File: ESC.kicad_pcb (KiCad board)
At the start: 2 copper layers, 44.5 x 36 mm, 68 parts, among them U1 DRV8300DRGER, U10 AP7381-33SA-7, U8 STM32G071GBU3TR, U9 UA78L10ACPK

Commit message: Fixed pin names
reset pins to apply proper net names
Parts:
- removed R21: 1K, Resistor_SMD:R_0402_1005Metric
- added R14: 1K, Resistor_SMD:R_0402_1005Metric, F.Cu at (119.5, 99.5)
- U8: footprint STM32:UFQFPN-28 -> STM32 G0:UFQFPN-28
- moved R5 8.45 mm to (99.0, 106.0), turned to 180 degrees
- moved R8 7.81 mm to (99.0, 104.0), turned to 0 degrees
- moved R6 7.41 mm to (97.0, 103.0), turned to 0 degrees
- moved R4 7.28 mm to (99.0, 105.0), turned to 180 degrees
- moved R9 6.53 mm to (99.0, 103.0), turned to 0 degrees
- moved C12 4.09 mm to (128.5, 121.5)
- moved R3 3.06 mm to (98.0, 94.5)
- moved C11 2.83 mm to (127.5, 98.0)
- moved R20 1.59 mm to (123.2, 99.4)
- renumbered TP3 to DShot1
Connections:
- net Net-(U8-PB4) renamed /Sub_ESC/MCU/DShotTXRX
- C11 pad 2: Net-(C11-Pad2) -> -BATT
- C28 pad 2: Net-(C28-Pad2) -> -BATT
- C29 pad 2: Net-(C29-Pad2) -> -BATT
- R10 pad 1: Net-(R10-Pad1) -> -BATT
- R3 pad 2: Net-(U1-GND) -> -BATT
- R6 pad 2: Net-(R10-Pad1) -> -BATT
- R8 pad 1: Net-(R10-Pad1) -> -BATT
- R9 pad 1: Net-(R10-Pad1) -> -BATT
- U1 pad 25: Net-(U1-GND) -> -BATT
- U1 pad 6: Net-(U1-GND) -> -BATT
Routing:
- net /Sub_ESC/MCU/SWD_IO: track 0.00 -> 16.7 mm
- net /Sub_ESC/Driver Output/ZC_C: track 0.00 -> 14.3 mm
- net /Sub_ESC/Driver Output/ZC_A: track 0.00 -> 12.6 mm
- net /Sub_ESC/MCU/SWD_CLK: track 0.00 -> 11.3 mm
- net /Sub_ESC/DShot: track 0.00 -> 7.32 mm
- net /Sub_ESC/Driver Output/PWM__L_A: track 3.69 -> 4.24 mm

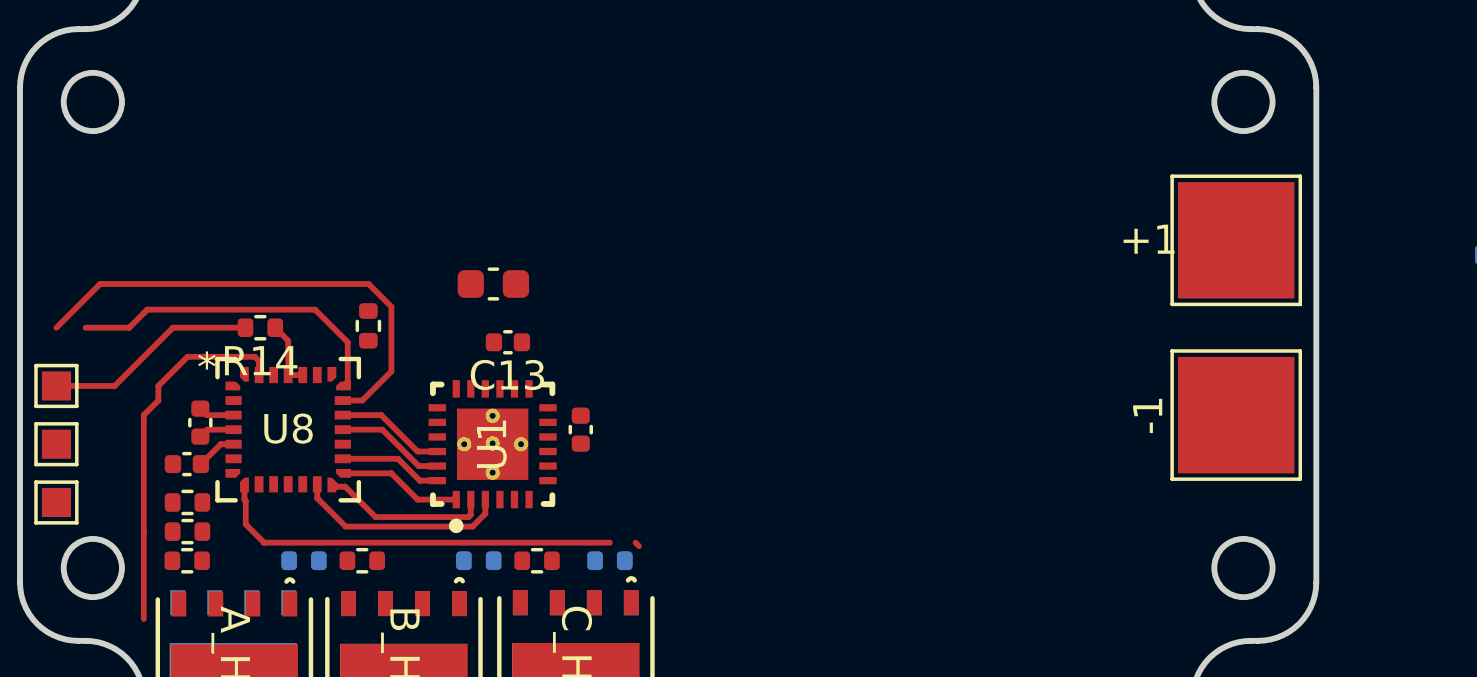
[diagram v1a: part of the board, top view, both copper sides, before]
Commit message: added additional layers and planes
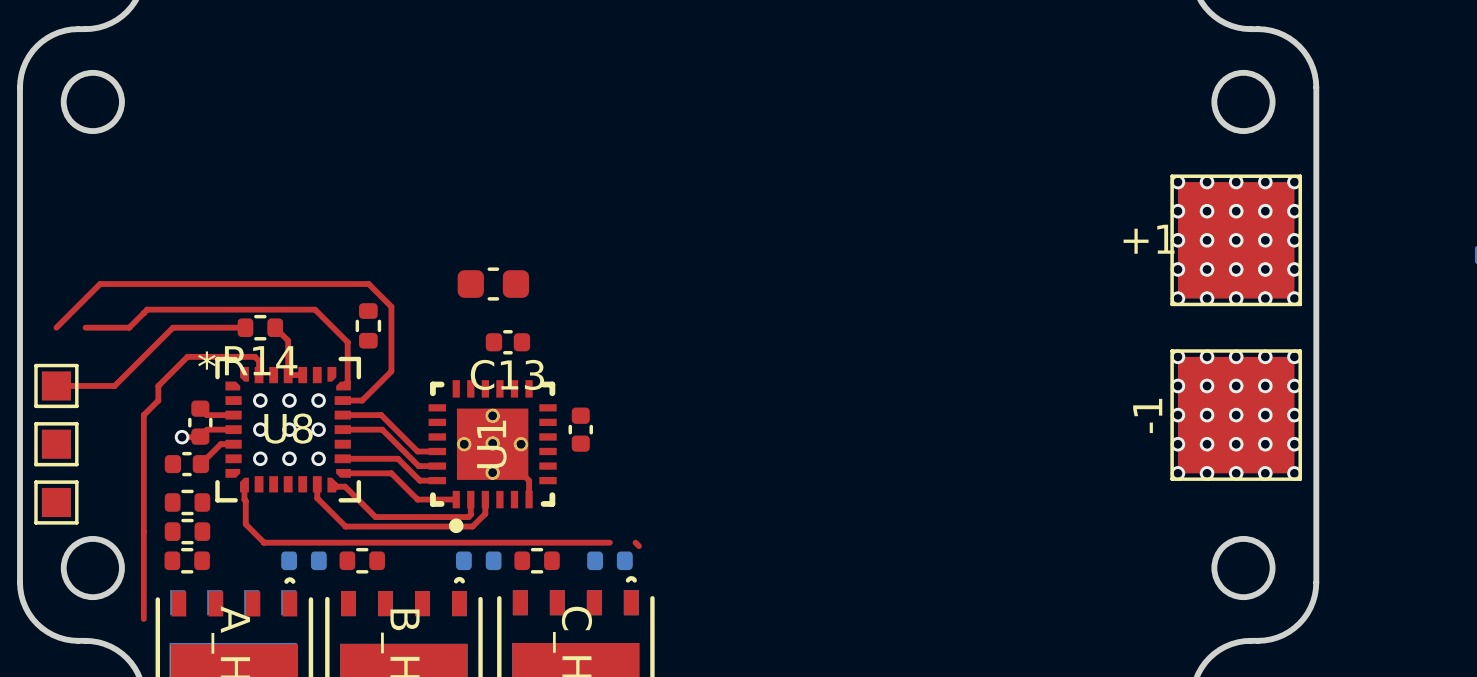
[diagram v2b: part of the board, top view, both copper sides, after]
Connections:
- U1 pad 26: (no net) -> -BATT
- U1 pad 27: (no net) -> -BATT
- U1 pad 28: (no net) -> -BATT
- U1 pad 29: (no net) -> -BATT
- U1 pad 30: (no net) -> -BATT
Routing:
- net -BATT: track 1.24 -> 4.29 mm, vias 0 -> 35
- net +BATT: vias 0 -> 25
- added copper zone on In2.Cu, net +BATT
- added copper zone on In1.Cu, net -BATT
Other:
- copper layers 2 -> 8

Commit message: more routing
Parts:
- C27, C28, C29, R10, R12, R13, R3, R7: moved to B.Cu
- moved C27 38.6 mm to (142.0, 98.8), turned to 180 degrees
- moved C28 38.6 mm to (142.0, 100.5), turned to 180 degrees
- moved C29 38.6 mm to (142.0, 102.2), turned to 180 degrees
- moved R4 32.0 mm to (131.0, 104.5)
- moved R5 32.0 mm to (131.0, 105.5)
- moved R6 32.0 mm to (129.0, 102.5)
- moved R8 32.0 mm to (131.0, 103.5)
- moved R9 32.0 mm to (131.0, 102.5)
- moved R3 28.5 mm to (124.5, 105.0)
- moved U10 27.6 mm to (136.5, 99.5), turned to 0 degrees
- moved R7 25.6 mm to (125.0, 106.5), turned to 0 degrees
- moved U9 20.2 mm to (143.5, 99.5)
- moved C12 18.7 mm to (131.5, 103.0)
- moved R12 17.4 mm to (120.2, 106.0)
- moved R13 16.1 mm to (119.5, 106.0)
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- renumbered B1 to A1, B_High1 to A_High1, B_Low1 to A_Low1, C30 to B1, C_High1 to B_High1, C_Low1 to B_Low1, A1 to C30, A_High1 to C_High1, A_Low1 to C_Low1, R_Gate_B_High1 to R_Gate_A_High1, R_Gate_B_Low1 to R_Gate_A_Low1, R_Gate_C_High1 to R_Gate_B_High1, R_Gate_C_Low1 to R_Gate_B_Low1, R_Gate_A_High1 to R_Gate_C_High1, R_Gate_A_Low1 to R_Gate_C_Low1
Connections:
- net /Sub_ESC/Driver Output/Half Bridge - 6S 50A - 2/BST_X renamed /Sub_ESC/Driver Output/BSTB
- net /Sub_ESC/Driver Output/Half Bridge - 6S 50A - 2/GATE_HIGH_X renamed /Sub_ESC/Driver Output/GHB
- net /Sub_ESC/Driver Output/Half Bridge - 6S 50A - 2/GATE_LOW_X renamed /Sub_ESC/Driver Output/GLB
- A1 pad 1: Net-(B1-Pad1) -> /Sub_ESC/Driver Output/A
- A_High1 pad 1: Net-(B1-Pad1) -> /Sub_ESC/Driver Output/A
- A_High1 pad 2: Net-(B1-Pad1) -> /Sub_ESC/Driver Output/A
- A_High1 pad 3: Net-(B1-Pad1) -> /Sub_ESC/Driver Output/A
- A_High1 pad 5: Net-(B_High1-DRAIN-Pad5) -> +BATT
- A_High1 pad 6: Net-(B_High1-DRAIN-Pad5) -> +BATT
- A_High1 pad 7: Net-(B_High1-DRAIN-Pad5) -> +BATT
- A_High1 pad 8: Net-(B_High1-DRAIN-Pad5) -> +BATT
- A_Low1 pad 1: Net-(B_Low1-SOURCE-Pad1) -> -BATT
- A_Low1 pad 2: Net-(B_Low1-SOURCE-Pad1) -> -BATT
- A_Low1 pad 3: Net-(B_Low1-SOURCE-Pad1) -> -BATT
- A_Low1 pad 5: Net-(B1-Pad1) -> /Sub_ESC/Driver Output/A
- A_Low1 pad 6: Net-(B1-Pad1) -> /Sub_ESC/Driver Output/A
- A_Low1 pad 7: Net-(B1-Pad1) -> /Sub_ESC/Driver Output/A
- A_Low1 pad 8: Net-(B1-Pad1) -> /Sub_ESC/Driver Output/A
- B1 pad 1: Net-(C14-Pad2) -> /Sub_ESC/Driver Output/B
- B_High1 pad 1: Net-(C14-Pad2) -> /Sub_ESC/Driver Output/B
- B_High1 pad 2: Net-(C14-Pad2) -> /Sub_ESC/Driver Output/B
- B_High1 pad 3: Net-(C14-Pad2) -> /Sub_ESC/Driver Output/B
- B_High1 pad 5: Net-(C_High1-DRAIN-Pad5) -> +BATT
- B_High1 pad 6: Net-(C_High1-DRAIN-Pad5) -> +BATT
- B_High1 pad 7: Net-(C_High1-DRAIN-Pad5) -> +BATT
- B_High1 pad 8: Net-(C_High1-DRAIN-Pad5) -> +BATT
- B_Low1 pad 1: Net-(C_Low1-SOURCE-Pad1) -> -BATT
- B_Low1 pad 2: Net-(C_Low1-SOURCE-Pad1) -> -BATT
- B_Low1 pad 3: Net-(C_Low1-SOURCE-Pad1) -> -BATT
- B_Low1 pad 5: Net-(C14-Pad2) -> /Sub_ESC/Driver Output/B
- B_Low1 pad 6: Net-(C14-Pad2) -> /Sub_ESC/Driver Output/B
- B_Low1 pad 7: Net-(C14-Pad2) -> /Sub_ESC/Driver Output/B
- B_Low1 pad 8: Net-(C14-Pad2) -> /Sub_ESC/Driver Output/B
- C12 pad 2: Net-(A1-Pad1) -> /Sub_ESC/Driver Output/C
- C13 pad 2: Net-(B1-Pad1) -> /Sub_ESC/Driver Output/A
- C14 pad 2: Net-(C14-Pad2) -> /Sub_ESC/Driver Output/B
- C28 pad 2: -BATT -> Net-(C28-Pad2)
- C29 pad 2: -BATT -> Net-(C29-Pad2)
- C30 pad 1: Net-(A1-Pad1) -> /Sub_ESC/Driver Output/C
- C_High1 pad 1: Net-(A1-Pad1) -> /Sub_ESC/Driver Output/C
- C_High1 pad 2: Net-(A1-Pad1) -> /Sub_ESC/Driver Output/C
- C_High1 pad 3: Net-(A1-Pad1) -> /Sub_ESC/Driver Output/C
- C_High1 pad 5: Net-(A_High1-DRAIN-Pad5) -> +BATT
- C_High1 pad 6: Net-(A_High1-DRAIN-Pad5) -> +BATT
- C_High1 pad 7: Net-(A_High1-DRAIN-Pad5) -> +BATT
- C_High1 pad 8: Net-(A_High1-DRAIN-Pad5) -> +BATT
- C_Low1 pad 1: Net-(A_Low1-SOURCE-Pad1) -> -BATT
- C_Low1 pad 2: Net-(A_Low1-SOURCE-Pad1) -> -BATT
- C_Low1 pad 3: Net-(A_Low1-SOURCE-Pad1) -> -BATT
- C_Low1 pad 5: Net-(A1-Pad1) -> /Sub_ESC/Driver Output/C
- C_Low1 pad 6: Net-(A1-Pad1) -> /Sub_ESC/Driver Output/C
- C_Low1 pad 7: Net-(A1-Pad1) -> /Sub_ESC/Driver Output/C
- C_Low1 pad 8: Net-(A1-Pad1) -> /Sub_ESC/Driver Output/C
- R1 pad 1: Net-(R1-Pad1) -> +BATT
- R2 pad 2: Net-(R2-Pad2) -> -BATT
- U1 pad 26: -BATT -> (no net)
- U1 pad 27: -BATT -> (no net)
- U1 pad 28: -BATT -> (no net)
- U1 pad 29: -BATT -> (no net)
- U1 pad 30: -BATT -> (no net)
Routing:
- net /Sub_ESC/Driver Output/A: track 0.00 -> 14.5 mm, vias 0 -> 18
- net /Sub_ESC/Driver Output/ZC_A: track 12.6 -> 5.61 mm
- net -BATT: track 4.29 -> 9.31 mm, vias 35 -> 36
- net /Sub_ESC/VGND: track 0.00 -> 4.45 mm
- net /Batt_Sense: track 0.01 -> 2.47 mm
- net +BATT: track 0.00 -> 0.49 mm, vias 25 -> 46
- net /Sub_ESC/Driver Output/C: vias 0 -> 18
- net /Sub_ESC/Driver Output/B: vias 0 -> 18
- added copper zone on F.Cu, net +BATT
- added copper zone on In3.Cu, net +BATT
- added copper zone on In6.Cu, net +BATT
- added copper zone on B.Cu, net -BATT
- added copper zone on In2.Cu, net -BATT
- added copper zone on In4.Cu, net -BATT
- added copper zone on In5.Cu, net -BATT
- removed copper zone on In2.Cu, net +BATT

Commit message: more routing and placement
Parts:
- removed DShot1, SWCLK1, SWDIO1: TestPoint, TestPoint:TestPoint_Pad_1.0x1.0mm
- added ?: , , F.Cu at (141.2, 106.2)
- added ?: , , F.Cu at (134.1, 108.0)
- added ?: , , F.Cu at (117.2, 107.9)
- added ?: , , F.Cu at (136.6, 108.0)
- added ?: , , F.Cu at (143.3, 108.0)
- added ?: , , F.Cu at (121.8, 107.8)
- added ?: , , F.Cu at (123.3, 106.2)
- added ?: , , F.Cu at (143.1, 106.2)
- added ?: , , F.Cu at (131.4, 107.9)
- added ?: , , F.Cu at (141.4, 108.0)
- added ?: , , F.Cu at (123.0, 107.9)
- added ?: , , F.Cu at (131.2, 106.2)
- added ?: , , F.Cu at (116.6, 107.9)
- added ?: , , F.Cu at (148.0, 106.2)
- added ?: , , F.Cu at (139.5, 108.0)
- added ?: , , F.Cu at (117.9, 107.8)
- added ?: , , F.Cu at (127.6, 107.9)
- added ?: , , F.Cu at (140.7, 108.0)
- added ?: , , F.Cu at (128.8, 107.9)
- added ?: , , F.Cu at (136.0, 108.0)
- added ?: , , F.Cu at (119.7, 107.9)
- added ?: , , F.Cu at (123.7, 107.8)
- added ?: , , F.Cu at (135.2, 106.2)
- added ?: , , F.Cu at (134.7, 108.0)
- added ?: , , F.Cu at (135.3, 108.0)
- added ?: , , F.Cu at (129.5, 107.9)
- added ?: , , F.Cu at (148.0, 107.9)
- added ?: , , F.Cu at (137.2, 108.0)
- added ?: , , F.Cu at (128.2, 107.9)
- added ?: , , F.Cu at (125.5, 107.8)
- added ?: , , F.Cu at (145.5, 108.0)
- added ?: , , F.Cu at (119.1, 107.9)
- added ?: , , F.Cu at (139.1, 106.2)
- added ?: , , F.Cu at (137.1, 106.2)
- added ?: , , F.Cu at (130.1, 107.9)
- added ?: , , F.Cu at (147.4, 107.9)
- added ?: , , F.Cu at (142.0, 108.0)
- added ?: , , F.Cu at (125.2, 106.2)
- added ?: , , F.Cu at (149.3, 107.9)
- added ?: , , F.Cu at (122.4, 107.9)
- added ?: , , F.Cu at (133.3, 106.2)
- added ?: , , F.Cu at (116.0, 107.9)
- added ?: , , F.Cu at (146.1, 107.9)
- added ?: , , F.Cu at (142.6, 108.0)
- added ?: , , F.Cu at (130.8, 107.9)
- added ?: , , F.Cu at (148.6, 107.9)
- added ?: , , F.Cu at (124.9, 107.9)
- added ?: , , F.Cu at (146.7, 107.9)
- added ?: , , F.Cu at (118.5, 107.9)
- added ?: , , F.Cu at (140.1, 108.0)
- added ?: , , F.Cu at (124.3, 107.8)
- added A_High2: High, Toshiba FET:SOP-ADVANCE_N_TOS, F.Cu at (136.0, 112.0)
- added A_High3: High, Toshiba FET:SOP-ADVANCE_N_TOS, F.Cu at (118.8, 88.2)
- added A_High4: High, Toshiba FET:SOP-ADVANCE_N_TOS, F.Cu at (136.8, 88.2)
- added A_Low2: Low, Toshiba FET:SOP-ADVANCE_N_TOS, B.Cu at (136.0, 110.9)
- added A_Low3: Low, Toshiba FET:SOP-ADVANCE_N_TOS, B.Cu at (118.8, 89.5)
- added A_Low4: Low, Toshiba FET:SOP-ADVANCE_N_TOS, B.Cu at (136.8, 89.2)
- added B_High2: High, Toshiba FET:SOP-ADVANCE_N_TOS, F.Cu at (142.0, 112.0)
- added B_High3: High, Toshiba FET:SOP-ADVANCE_N_TOS, F.Cu at (124.8, 88.2)
- added B_High4: High, Toshiba FET:SOP-ADVANCE_N_TOS, F.Cu at (142.8, 88.2)
- added B_Low2: Low, Toshiba FET:SOP-ADVANCE_N_TOS, B.Cu at (142.0, 110.9)
- added B_Low3: Low, Toshiba FET:SOP-ADVANCE_N_TOS, B.Cu at (124.8, 89.5)
- added B_Low4: Low, Toshiba FET:SOP-ADVANCE_N_TOS, B.Cu at (142.6, 89.2)
- added C30: C_Small, Capacitor_SMD:C_0603_1608Metric, F.Cu at (164.3, 44.9)
- added C31: 0.1 uF, Capacitor_SMD:C_0402_1005Metric, F.Cu at (183.1, 95.3)
- added C32: 0.1 uF, Capacitor_SMD:C_0402_1005Metric, F.Cu at (147.8, 107.8)
- added C34: 0.1 uF, Capacitor_SMD:C_0402_1005Metric, F.Cu at (149.2, 106.0)
- added C35: 10uF, Capacitor_SMD:C_0402_1005Metric, F.Cu at (142.9, 107.0)
- added C36: .1uF, Capacitor_SMD:C_0402_1005Metric, F.Cu at (144.0, 108.0)
- added C37: C_Small, Capacitor_SMD:C_0603_1608Metric, F.Cu at (188.0, 44.9)
- added C38: 0.1 uF, Capacitor_SMD:C_0402_1005Metric, F.Cu at (125.5, 92.5)
- added C39: 0.1 uF, Capacitor_SMD:C_0402_1005Metric, F.Cu at (127.0, 95.0)
- added C40: 0.1 uF, Capacitor_SMD:C_0402_1005Metric, F.Cu at (129.0, 93.8)
- added C41: 10uF, Capacitor_SMD:C_0402_1005Metric, F.Cu at (126.9, 95.5)
- added C42: .1uF, Capacitor_SMD:C_0402_1005Metric, F.Cu at (126.9, 97.4)
- added C43: C_Small, Capacitor_SMD:C_0603_1608Metric, F.Cu at (176.2, 44.9)
- added C44: 0.1 uF, Capacitor_SMD:C_0402_1005Metric, F.Cu at (190.9, 95.3)
- added C45: 0.1 uF, Capacitor_SMD:C_0402_1005Metric, F.Cu at (198.7, 95.3)
- added C46: 0.1 uF, Capacitor_SMD:C_0402_1005Metric, F.Cu at (148.5, 94.2)
- added C47: 10uF, Capacitor_SMD:C_0402_1005Metric, F.Cu at (144.4, 95.5)
- added C48: .1uF, Capacitor_SMD:C_0402_1005Metric, F.Cu at (144.4, 97.4)
- added C_High2: High, Toshiba FET:SOP-ADVANCE_N_TOS, F.Cu at (148.0, 112.0)
- added C_High3: High, Toshiba FET:SOP-ADVANCE_N_TOS, F.Cu at (130.6, 88.4)
- added C_High4: High, Toshiba FET:SOP-ADVANCE_N_TOS, F.Cu at (148.7, 88.1)
- added C_Low2: Low, Toshiba FET:SOP-ADVANCE_N_TOS, B.Cu at (148.0, 110.8)
- added C_Low3: Low, Toshiba FET:SOP-ADVANCE_N_TOS, B.Cu at (130.6, 89.4)
- added C_Low4: Low, Toshiba FET:SOP-ADVANCE_N_TOS, B.Cu at (148.6, 89.2)
- added J1: Conn_01x07, Connector_JST:JST_GH_BM07B-GHS-TBT_1x07-1MP_P1.25mm_Vertical, F.Cu at (114.7, 99.8)
- added J2: Conn_01x07, Connector_JST:JST_GH_BM07B-GHS-TBT_1x07-1MP_P1.25mm_Vertical, B.Cu at (114.6, 99.7)
- added R16: 100K Ohm, Resistor_SMD:R_0402_1005Metric, F.Cu at (158.0, 44.6)
- added R17: 10K, Resistor_SMD:R_0402_1005Metric, F.Cu at (158.0, 46.6)
- added R18: 10K, Resistor_SMD:R_0402_1005Metric, F.Cu at (158.0, 48.6)
- added R19: 1M, Resistor_SMD:R_0402_1005Metric, F.Cu at (158.0, 50.6)
- added R20: 10K, Resistor_SMD:R_0402_1005Metric, F.Cu at (158.0, 52.6)
- added R21: 1K, Resistor_SMD:R_0402_1005Metric, F.Cu at (158.0, 54.6)
- added R22: 1K, Resistor_SMD:R_0402_1005Metric, F.Cu at (160.9, 44.6)
- added R23: 1K, Resistor_SMD:R_0402_1005Metric, F.Cu at (160.9, 46.6)
- added R24: 10K, Resistor_SMD:R_0402_1005Metric, F.Cu at (160.9, 48.6)
- added R25: 10K, Resistor_SMD:R_0402_1005Metric, F.Cu at (160.9, 50.6)
- added R26: 10K, Resistor_SMD:R_0402_1005Metric, F.Cu at (160.9, 52.6)
- added R27: 10K, Resistor_SMD:R_0402_1005Metric, F.Cu at (143.0, 103.0)
- added R28: 1K, Resistor_SMD:R_0402_1005Metric, F.Cu at (143.0, 105.0)
- added R29: 100K Ohm, Resistor_SMD:R_0402_1005Metric, F.Cu at (181.6, 44.6)
- added R30: 10K, Resistor_SMD:R_0402_1005Metric, F.Cu at (181.6, 46.6)
- added R31: 10K, Resistor_SMD:R_0402_1005Metric, F.Cu at (181.6, 48.6)
- added R32: 1M, Resistor_SMD:R_0402_1005Metric, F.Cu at (181.6, 50.6)
- added R33: 10K, Resistor_SMD:R_0402_1005Metric, F.Cu at (181.6, 52.6)
- added R34: 1K, Resistor_SMD:R_0402_1005Metric, F.Cu at (181.6, 54.6)
- added R35: 1K, Resistor_SMD:R_0402_1005Metric, F.Cu at (184.5, 44.6)
- added R36: 1K, Resistor_SMD:R_0402_1005Metric, F.Cu at (184.5, 46.6)
- added R37: 10K, Resistor_SMD:R_0402_1005Metric, F.Cu at (184.5, 48.6)
- added R38: 10K, Resistor_SMD:R_0402_1005Metric, F.Cu at (184.5, 50.6)
- added R39: 10K, Resistor_SMD:R_0402_1005Metric, F.Cu at (184.5, 52.6)
- added R40: 10K, Resistor_SMD:R_0402_1005Metric, F.Cu at (127.0, 92.2)
- added R41: 1K, Resistor_SMD:R_0402_1005Metric, F.Cu at (127.0, 93.5)
- added R42: 100K Ohm, Resistor_SMD:R_0402_1005Metric, F.Cu at (169.8, 44.6)
- added R43: 10K, Resistor_SMD:R_0402_1005Metric, F.Cu at (169.8, 46.6)
- added R44: 10K, Resistor_SMD:R_0402_1005Metric, F.Cu at (169.8, 48.6)
- added R45: 1M, Resistor_SMD:R_0402_1005Metric, F.Cu at (169.8, 50.6)
- added R46: 10K, Resistor_SMD:R_0402_1005Metric, F.Cu at (169.8, 52.6)
- added R47: 1K, Resistor_SMD:R_0402_1005Metric, F.Cu at (169.8, 54.6)
- added R48: 1K, Resistor_SMD:R_0402_1005Metric, F.Cu at (172.7, 44.6)
- added R49: 1K, Resistor_SMD:R_0402_1005Metric, F.Cu at (172.7, 46.6)
- added R50: 10K, Resistor_SMD:R_0402_1005Metric, F.Cu at (172.7, 48.6)
- added R51: 10K, Resistor_SMD:R_0402_1005Metric, F.Cu at (172.7, 50.6)
- added R52: 10K, Resistor_SMD:R_0402_1005Metric, F.Cu at (172.7, 52.6)
- added R53: 10K, Resistor_SMD:R_0402_1005Metric, F.Cu at (144.5, 91.5)
- added R54: 1K, Resistor_SMD:R_0402_1005Metric, F.Cu at (144.5, 93.5)
- added R_Gate_A_High2: 10 Ohm, Resistor_SMD:R_0402_1005Metric, F.Cu at (180.2, 95.3)
- added R_Gate_A_High3: 10 Ohm, Resistor_SMD:R_0402_1005Metric, F.Cu at (133.2, 94.5)
- added R_Gate_A_High4: 10 Ohm, Resistor_SMD:R_0402_1005Metric, F.Cu at (188.0, 95.3)
- added R_Gate_A_Low2: 10 Ohm, Resistor_SMD:R_0402_1005Metric, F.Cu at (180.2, 97.3)
- added R_Gate_A_Low3: 10 Ohm, Resistor_SMD:R_0402_1005Metric, F.Cu at (133.2, 96.5)
- added R_Gate_A_Low4: 10 Ohm, Resistor_SMD:R_0402_1005Metric, F.Cu at (188.0, 97.3)
- added R_Gate_B_High2: 10 Ohm, Resistor_SMD:R_0402_1005Metric, F.Cu at (140.2, 104.5)
- added R_Gate_B_High3: 10 Ohm, Resistor_SMD:R_0402_1005Metric, F.Cu at (118.8, 93.2)
- added R_Gate_B_High4: 10 Ohm, Resistor_SMD:R_0402_1005Metric, F.Cu at (168.5, 116.5)
- added R_Gate_B_Low2: 10 Ohm, Resistor_SMD:R_0402_1005Metric, F.Cu at (140.2, 106.5)
- added R_Gate_B_Low3: 10 Ohm, Resistor_SMD:R_0402_1005Metric, F.Cu at (121.0, 92.8)
- added R_Gate_B_Low4: 10 Ohm, Resistor_SMD:R_0402_1005Metric, F.Cu at (143.8, 94.0)
- added R_Gate_C_High2: 10 Ohm, Resistor_SMD:R_0402_1005Metric, F.Cu at (148.0, 107.2)
- added R_Gate_C_High3: 10 Ohm, Resistor_SMD:R_0402_1005Metric, F.Cu at (126.3, 93.5)
- added R_Gate_C_High4: 10 Ohm, Resistor_SMD:R_0402_1005Metric, F.Cu at (195.8, 95.3)
- added R_Gate_C_Low2: 10 Ohm, Resistor_SMD:R_0402_1005Metric, F.Cu at (146.3, 106.5)
- added R_Gate_C_Low3: 10 Ohm, Resistor_SMD:R_0402_1005Metric, F.Cu at (126.3, 95.5)
- added R_Gate_C_Low4: 10 Ohm, Resistor_SMD:R_0402_1005Metric, F.Cu at (195.8, 97.3)
- added U10: STM32G071GBU3TR, STM32 G0:UFQFPN-28, F.Cu at (140.0, 93.5)
- added U5: DRV8300DRGER, TI Driver:RGE0024B-MFG, F.Cu at (145.5, 104.5)
- added U6: STM32G071GBU3TR, STM32 G0:UFQFPN-28, F.Cu at (138.5, 105.0)
- added U7: DRV8300DRGER, TI Driver:RGE0024B-MFG, F.Cu at (125.0, 94.0)
- added U8: STM32G071GBU3TR, STM32 G0:UFQFPN-28, F.Cu at (122.5, 93.5)
- added U9: DRV8300DRGER, TI Driver:RGE0024B-MFG, F.Cu at (146.1, 94.2)
- moved C13 28.9 mm to (143.2, 105.2), turned to -90 degrees
- moved C15 26.6 mm to (123.3, 105.3), turned to -90 degrees
- moved C11 26.2 mm to (141.2, 105.3), turned to -90 degrees
- moved C14 24.6 mm to (142.8, 95.3), turned to 90 degrees
- moved C17 24.2 mm to (125.3, 105.3), turned to -90 degrees
- moved C12 24.0 mm to (124.8, 95.2), turned to 90 degrees
- moved C9 23.9 mm to (139.2, 105.2), turned to -90 degrees
- moved C19 23.3 mm to (148.0, 105.2), turned to -90 degrees
- moved C7 22.1 mm to (137.2, 105.2), turned to -90 degrees
- moved C16 21.7 mm to (140.8, 95.2), turned to 90 degrees
- moved C10 21.2 mm to (126.8, 95.2), turned to 90 degrees
- moved C5 20.8 mm to (135.2, 105.2), turned to -90 degrees
- moved C21 20.6 mm to (131.2, 105.2), turned to -90 degrees
- moved C23 20.3 mm to (133.2, 105.3), turned to -90 degrees
- moved C18 19.3 mm to (138.8, 95.2), turned to 90 degrees
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- renumbered C30 to A1, A1 to A2, B1 to A3, C29 to C1, C4 to C10, C20 to C11, C5 to C12, C21 to C13, C6 to C14, C22 to C15, C7 to C16, C23 to C17, C8 to C18, C24 to C19, C27 to C2, C9 to C20, C25 to C21, C10 to C22, C26 to C23, C11 to C24, C12 to C25, C13 to C26, C14 to C27, C15 to C28, C16 to C29, C28 to C3, C1 to C4, C17 to C5, C2 to C6, C18 to C7, C3 to C8, C19 to C9, R20 to R14, R14 to R15, U9 to U1, U10 to U2, U1 to U3, U8 to U4
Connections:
- net /Sub_ESC/MCU/SWD_CLK renamed /SWD_CLK_1
- C1 pad 2: Net-(C29-Pad2) -> -BATT
- C10 pad 1: Net-(C1-Pad1) -> +BATT
- C10 pad 2: Net-(C1-Pad2) -> -BATT
- C11 pad 1: Net-(C17-Pad1) -> +BATT
- C11 pad 2: Net-(C17-Pad2) -> -BATT
- C12 pad 1: Net-(C1-Pad1) -> +BATT
- C12 pad 2: Net-(C1-Pad2) -> -BATT
- C13 pad 1: Net-(C17-Pad1) -> +BATT
- C13 pad 2: Net-(C17-Pad2) -> -BATT
- C14 pad 1: Net-(C1-Pad1) -> +BATT
- C14 pad 2: Net-(C1-Pad2) -> -BATT
- C15 pad 1: Net-(C17-Pad1) -> +BATT
- C15 pad 2: Net-(C17-Pad2) -> -BATT
- C16 pad 1: Net-(C1-Pad1) -> +BATT
- C16 pad 2: Net-(C1-Pad2) -> -BATT
- C17 pad 1: Net-(C17-Pad1) -> +BATT
- C17 pad 2: Net-(C17-Pad2) -> -BATT
- C18 pad 1: Net-(C1-Pad1) -> +BATT
- C18 pad 2: Net-(C1-Pad2) -> -BATT
- C19 pad 1: Net-(C17-Pad1) -> +BATT
- C19 pad 2: Net-(C17-Pad2) -> -BATT
- C20 pad 1: Net-(C1-Pad1) -> +BATT
- C20 pad 2: Net-(C1-Pad2) -> -BATT
- C21 pad 1: Net-(C17-Pad1) -> +BATT
- C21 pad 2: Net-(C17-Pad2) -> -BATT
- C22 pad 1: Net-(C1-Pad1) -> +BATT
- C22 pad 2: Net-(C1-Pad2) -> -BATT
- C23 pad 1: Net-(C17-Pad1) -> +BATT
- C23 pad 2: Net-(C17-Pad2) -> -BATT
- C3 pad 2: Net-(C28-Pad2) -> -BATT
- C4 pad 1: Net-(C1-Pad1) -> +BATT
- C4 pad 2: Net-(C1-Pad2) -> -BATT
- C5 pad 1: Net-(C17-Pad1) -> +BATT
- C5 pad 2: Net-(C17-Pad2) -> -BATT
- C6 pad 1: Net-(C1-Pad1) -> +BATT
- C6 pad 2: Net-(C1-Pad2) -> -BATT
- C7 pad 1: Net-(C17-Pad1) -> +BATT
- C7 pad 2: Net-(C17-Pad2) -> -BATT
- C8 pad 1: Net-(C1-Pad1) -> +BATT
- C8 pad 2: Net-(C1-Pad2) -> -BATT
- C9 pad 1: Net-(C17-Pad1) -> +BATT
- C9 pad 2: Net-(C17-Pad2) -> -BATT
- R15 pad 2: /Sub_ESC/DShot -> /DShot1
- U3 pad 26: (no net) -> -BATT
- U3 pad 27: (no net) -> -BATT
- U3 pad 28: (no net) -> -BATT
- U3 pad 29: (no net) -> -BATT
- U3 pad 30: (no net) -> -BATT
- U4 pad 20: /Sub_ESC/MCU/SWD_IO -> /SWD_IO_1
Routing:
- net /Sub_ESC/MCU/SWD_IO: track 16.7 -> 0.00 mm
- net /SWD_IO_1: track 0.00 -> 16.7 mm
- net /SWD_CLK_1: track 11.3 -> 0.00 mm
- net (no net): track 0.17 -> 11.5 mm
- net /Sub_ESC/DShot: track 7.32 -> 0.00 mm
- net /DShot1: track 0.00 -> 7.32 mm
- net /Sub_ESC/Driver Output/A: vias 18 -> 15
- net +BATT: vias 46 -> 67
- added copper zone on In2.Cu, net +BATT
- added copper zone on In4.Cu, net +BATT
- added copper zone on In3.Cu, net -BATT
- added copper zone on B.Cu, net /Sub_ESC/Driver Output/A
- added copper zone on F.Cu, net /Sub_ESC/Driver Output/A
- added copper zone on In1.Cu, net /Sub_ESC/Driver Output/A
- added copper zone on In2.Cu, net /Sub_ESC/Driver Output/A
- added copper zone on In3.Cu, net /Sub_ESC/Driver Output/A
- added copper zone on In4.Cu, net /Sub_ESC/Driver Output/A
- added copper zone on In5.Cu, net /Sub_ESC/Driver Output/A
- added copper zone on In6.Cu, net /Sub_ESC/Driver Output/A
- added copper zone on B.Cu, net /Sub_ESC/Driver Output/B
- added copper zone on F.Cu, net /Sub_ESC/Driver Output/B
- added copper zone on In1.Cu, net /Sub_ESC/Driver Output/B
- added copper zone on In2.Cu, net /Sub_ESC/Driver Output/B
- added copper zone on In3.Cu, net /Sub_ESC/Driver Output/B
- added copper zone on In4.Cu, net /Sub_ESC/Driver Output/B
- added copper zone on In5.Cu, net /Sub_ESC/Driver Output/B
- added copper zone on In6.Cu, net /Sub_ESC/Driver Output/B
- added copper zone on B.Cu, net /Sub_ESC/Driver Output/C
- added copper zone on F.Cu, net /Sub_ESC/Driver Output/C
- added copper zone on In1.Cu, net /Sub_ESC/Driver Output/C
- added copper zone on In2.Cu, net /Sub_ESC/Driver Output/C
- added copper zone on In3.Cu, net /Sub_ESC/Driver Output/C
- added copper zone on In4.Cu, net /Sub_ESC/Driver Output/C
- added copper zone on In5.Cu, net /Sub_ESC/Driver Output/C
- added copper zone on In6.Cu, net /Sub_ESC/Driver Output/C
- removed copper zone on In3.Cu, net +BATT
- removed copper zone on In2.Cu, net -BATT
- removed copper zone on In4.Cu, net -BATT
